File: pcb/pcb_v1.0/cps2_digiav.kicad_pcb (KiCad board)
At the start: 2 copper layers, 103.4 x 48.7 mm, 128 parts, among them J1 Conn_02x05, J2 Conn_02x05, J4 HDMI_CONN, P1 JTAG_CONN, U1 ADV7513, U10 S25FL116K, U12 TLV70012, U13 TLV70025, U14 TLV70012, U15 TLV70018, U16 TLV70018, U2 EP4CE15E22, U3 74LVC245, U4 74LVC245, U5 74LVC245, U6 SI5351C-B, U7 TC1262-3.3VDBTR, U8 TLV70033, U9 SN74LVC3G17

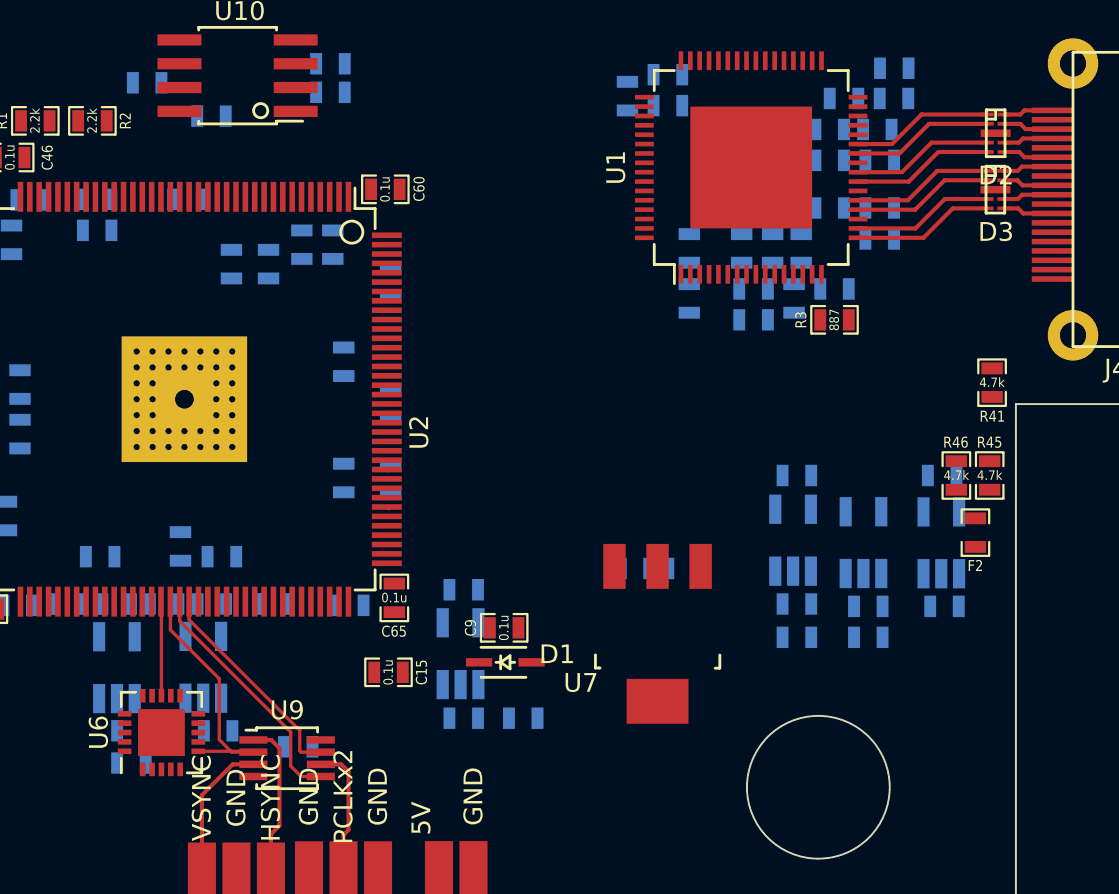
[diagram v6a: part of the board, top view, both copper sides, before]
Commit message: fix schematic and library linkage issues
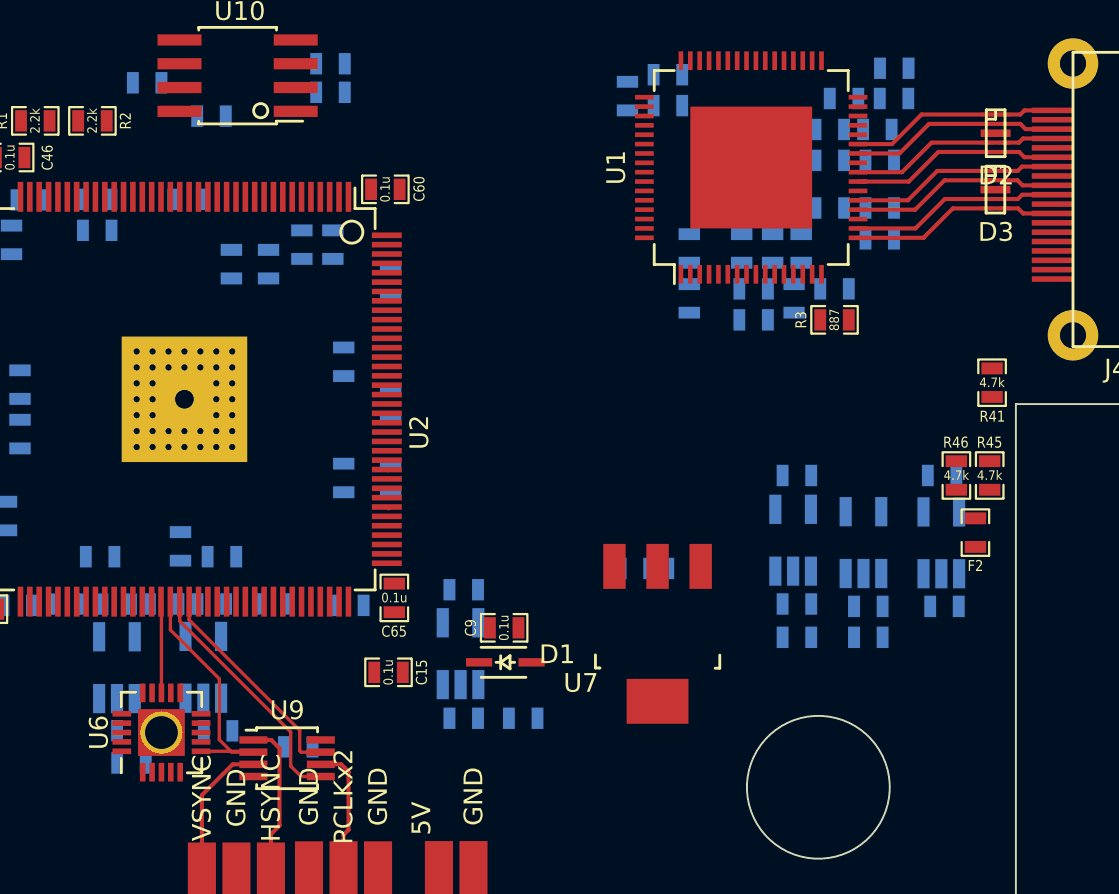
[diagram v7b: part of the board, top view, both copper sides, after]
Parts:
- D2, D3: footprint Custom_OSSC:SLP2510P8 -> custom_components:SLP2510P8
- U10: value S25FL116K -> IS25LP016D-JBLE
- U6: footprint Housings_DFN_QFN:QFN-20-1EP_4x4mm_Pitch0.5mm -> custom_components:QFN-20-1EP_4x4mm_Pitch0.5mm_Handsoldering
- U7: value TC1262-3.3VDBTR -> AP7361
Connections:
- net /hdmitx1/AVDD3V3 renamed /A33VDD
- D2 pad 10: Net-(D2-Pad10) -> /hdmitx1/TX2+
- D2 pad 6: Net-(D2-Pad6) -> /hdmitx1/TX1-
- D2 pad 7: Net-(D2-Pad7) -> /hdmitx1/TX1+
- D2 pad 8: (no net) -> Net-(D2-Pad8)
- D2 pad 9: Net-(D2-Pad9) -> /hdmitx1/TX2-
- D3 pad 10: Net-(D3-Pad10) -> /hdmitx1/TX0+
- D3 pad 6: Net-(D3-Pad6) -> /hdmitx1/TXC-
- D3 pad 7: Net-(D3-Pad7) -> /hdmitx1/TXC+
- D3 pad 8: (no net) -> Net-(D3-Pad8)
- D3 pad 9: Net-(D3-Pad9) -> /hdmitx1/TX0-
- FB1 pad 1: Net-(C13-Pad1) -> /hdmitx1/AVDD1V8
- FB1 pad 2: /hdmitx1/AVDD1V8 -> Net-(C13-Pad1)
- FB2 pad 1: Net-(C12-Pad1) -> /hdmitx1/AVDD1V8
- FB2 pad 2: /hdmitx1/AVDD1V8 -> Net-(C12-Pad1)
- FB3 pad 1: /hdmitx1/DVDD1V8 -> Net-(C10-Pad1)
- FB3 pad 2: Net-(C10-Pad1) -> /hdmitx1/DVDD1V8
- FB4 pad 1: /hdmitx1/DVDD3V3 -> Net-(C11-Pad1)
- FB4 pad 2: Net-(C11-Pad1) -> /hdmitx1/DVDD3V3
- J1 pad 1: (no net) -> Net-(J1-Pad1)
- J2 pad 1: (no net) -> Net-(J2-Pad1)
- J4 pad 1: Net-(D2-Pad10) -> /hdmitx1/TX2+
- J4 pad 10: Net-(D3-Pad7) -> /hdmitx1/TXC+
- J4 pad 12: Net-(D3-Pad6) -> /hdmitx1/TXC-
- J4 pad 13: (no net) -> Net-(J4-Pad13)
- J4 pad 14: (no net) -> Net-(J4-Pad14)
- J4 pad 3: Net-(D2-Pad9) -> /hdmitx1/TX2-
- J4 pad 4: Net-(D2-Pad7) -> /hdmitx1/TX1+
- J4 pad 6: Net-(D2-Pad6) -> /hdmitx1/TX1-
- J4 pad 7: Net-(D3-Pad10) -> /hdmitx1/TX0+
- J4 pad 9: Net-(D3-Pad9) -> /hdmitx1/TX0-
- P1 pad 6: (no net) -> Net-(P1-Pad6)
- P1 pad 7: (no net) -> Net-(P1-Pad7)
- P1 pad 8: (no net) -> Net-(P1-Pad8)
- U1 pad 3: (no net) -> Net-(U1-Pad3)
- U1 pad 30: (no net) -> Net-(U1-Pad30)
- U1 pad 32: (no net) -> Net-(U1-Pad32)
- U1 pad 6: (no net) -> Net-(U1-Pad6)
- U1 pad 7: (no net) -> Net-(U1-Pad7)
- U1 pad 8: (no net) -> Net-(U1-Pad8)
- U12 pad 4: (no net) -> Net-(U12-Pad4)
- U13 pad 4: (no net) -> Net-(U13-Pad4)
- U14 pad 4: (no net) -> Net-(U14-Pad4)
- U15 pad 4: (no net) -> Net-(U15-Pad4)
- U16 pad 4: (no net) -> Net-(U16-Pad4)
- U2 pad 28: (no net) -> Net-(U2-Pad28)
- U2 pad 32: (no net) -> Net-(U2-Pad32)
- U2 pad 33: (no net) -> Net-(U2-Pad33)
- U2 pad 76: (no net) -> Net-(U2-Pad76)
- U2 pad 77: (no net) -> Net-(U2-Pad77)
- U2 pad 80: (no net) -> Net-(U2-Pad80)
- U2 pad 83: (no net) -> Net-(U2-Pad83)
- U5 pad 11: (no net) -> Net-(U5-Pad11)
- U5 pad 12: (no net) -> Net-(U5-Pad12)
- U5 pad 13: (no net) -> Net-(U5-Pad13)
- U5 pad 7: (no net) -> Net-(U5-Pad7)
- U5 pad 8: (no net) -> Net-(U5-Pad8)
- U5 pad 9: (no net) -> Net-(U5-Pad9)
- U6 pad 1: (no net) -> Net-(U6-Pad1)
- U6 pad 12: (no net) -> Net-(U6-Pad12)
- U6 pad 15: (no net) -> Net-(U6-Pad15)
- U6 pad 16: (no net) -> Net-(U6-Pad16)
- U6 pad 17: (no net) -> Net-(U6-Pad17)
- U6 pad 19: (no net) -> Net-(U6-Pad19)
- U6 pad 2: (no net) -> Net-(U6-Pad2)
- U6 pad 8: (no net) -> Net-(U6-Pad8)
- U6 pad 9: (no net) -> Net-(U6-Pad9)
- U8 pad 4: (no net) -> Net-(U8-Pad4)
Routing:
- net /hdmitx1/TX0-: track 7.53 -> 11.1 mm
- net /hdmitx1/TXC-: track 7.53 -> 11.1 mm
- net /hdmitx1/TX2-: track 7.55 -> 11.1 mm
- net /hdmitx1/TX1-: track 7.55 -> 11.1 mm
- net /hdmitx1/TXC+: track 7.53 -> 11.1 mm
- net /hdmitx1/TX0+: track 7.53 -> 11.1 mm
- net /hdmitx1/TX1+: track 7.55 -> 11.1 mm
- net /hdmitx1/TX2+: track 7.55 -> 11.1 mm
- net Net-(D3-Pad9): track 2.70 -> 0.00 mm
- net Net-(D3-Pad6): track 2.70 -> 0.00 mm
- net Net-(D2-Pad9): track 2.69 -> 0.00 mm
- net Net-(D2-Pad6): track 2.69 -> 0.00 mm
- net Net-(D3-Pad7): track 2.69 -> 0.00 mm
- net Net-(D3-Pad10): track 2.69 -> 0.00 mm
- net Net-(D2-Pad7): track 2.67 -> 0.00 mm
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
